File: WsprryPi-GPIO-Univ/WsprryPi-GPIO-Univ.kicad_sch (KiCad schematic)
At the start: 11 parts, among them J11 GPIO, J21 GPIO Select, J81 Conn_01x04, J82 Conn_01x04, J83 SMA_Adafruit_1865, SW11 Switch

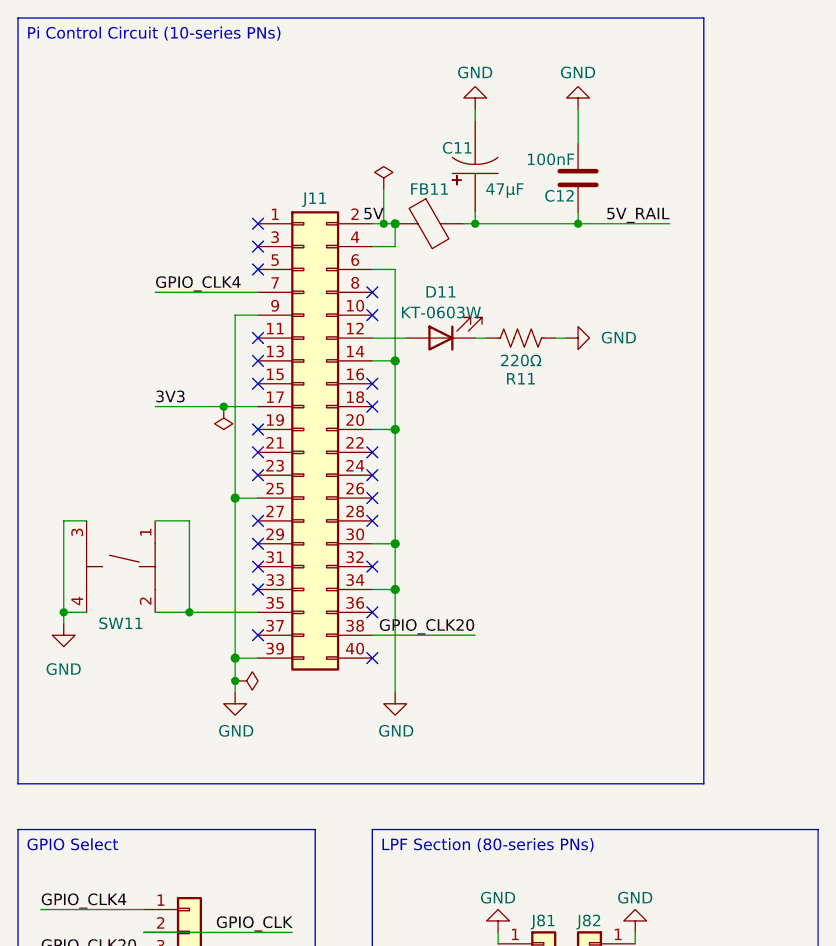
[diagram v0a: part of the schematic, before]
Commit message: Rename GPIO project and document amplifier requirements
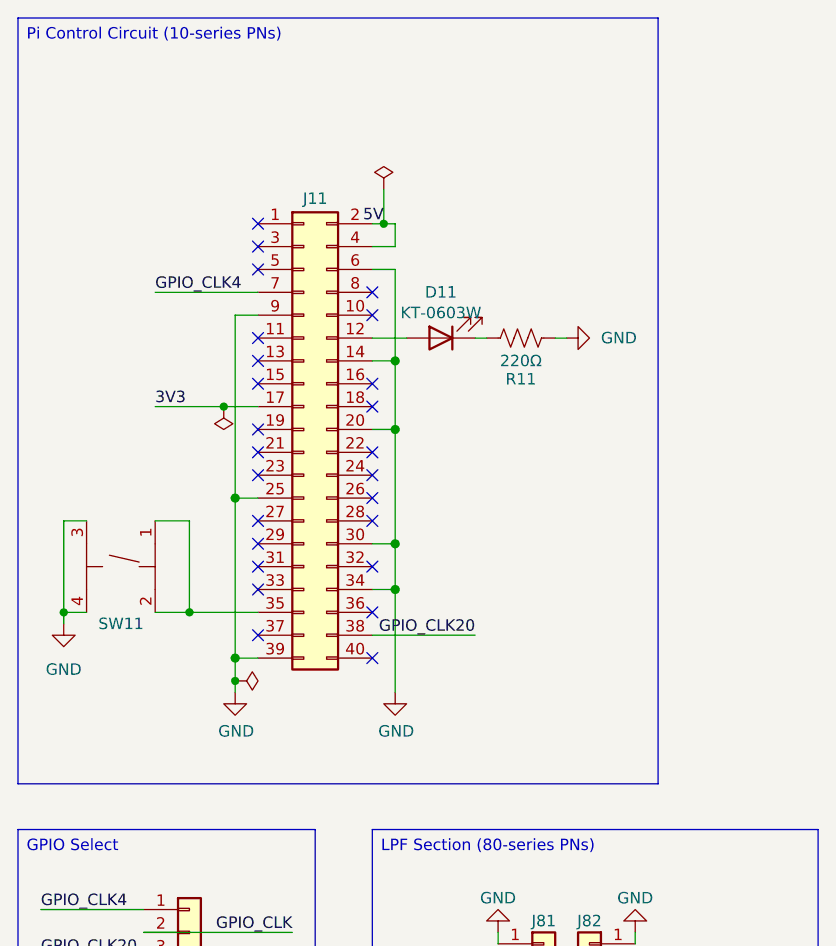
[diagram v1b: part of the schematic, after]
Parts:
- removed C11: 47µF, Wsprry Pi:CAP-SMD_BD6.3-L6.6-W6.6-FD, symbol Wsprry Pi:EEEFK1V470P
- removed C12: 100nF, Wsprry Pi:C_0603_1608Metric, symbol Wsprry Pi:C
- removed FB11: 600Ω@100MHz, Wsprry Pi:L_0603_1608Metric, symbol Wsprry Pi:FerriteBead

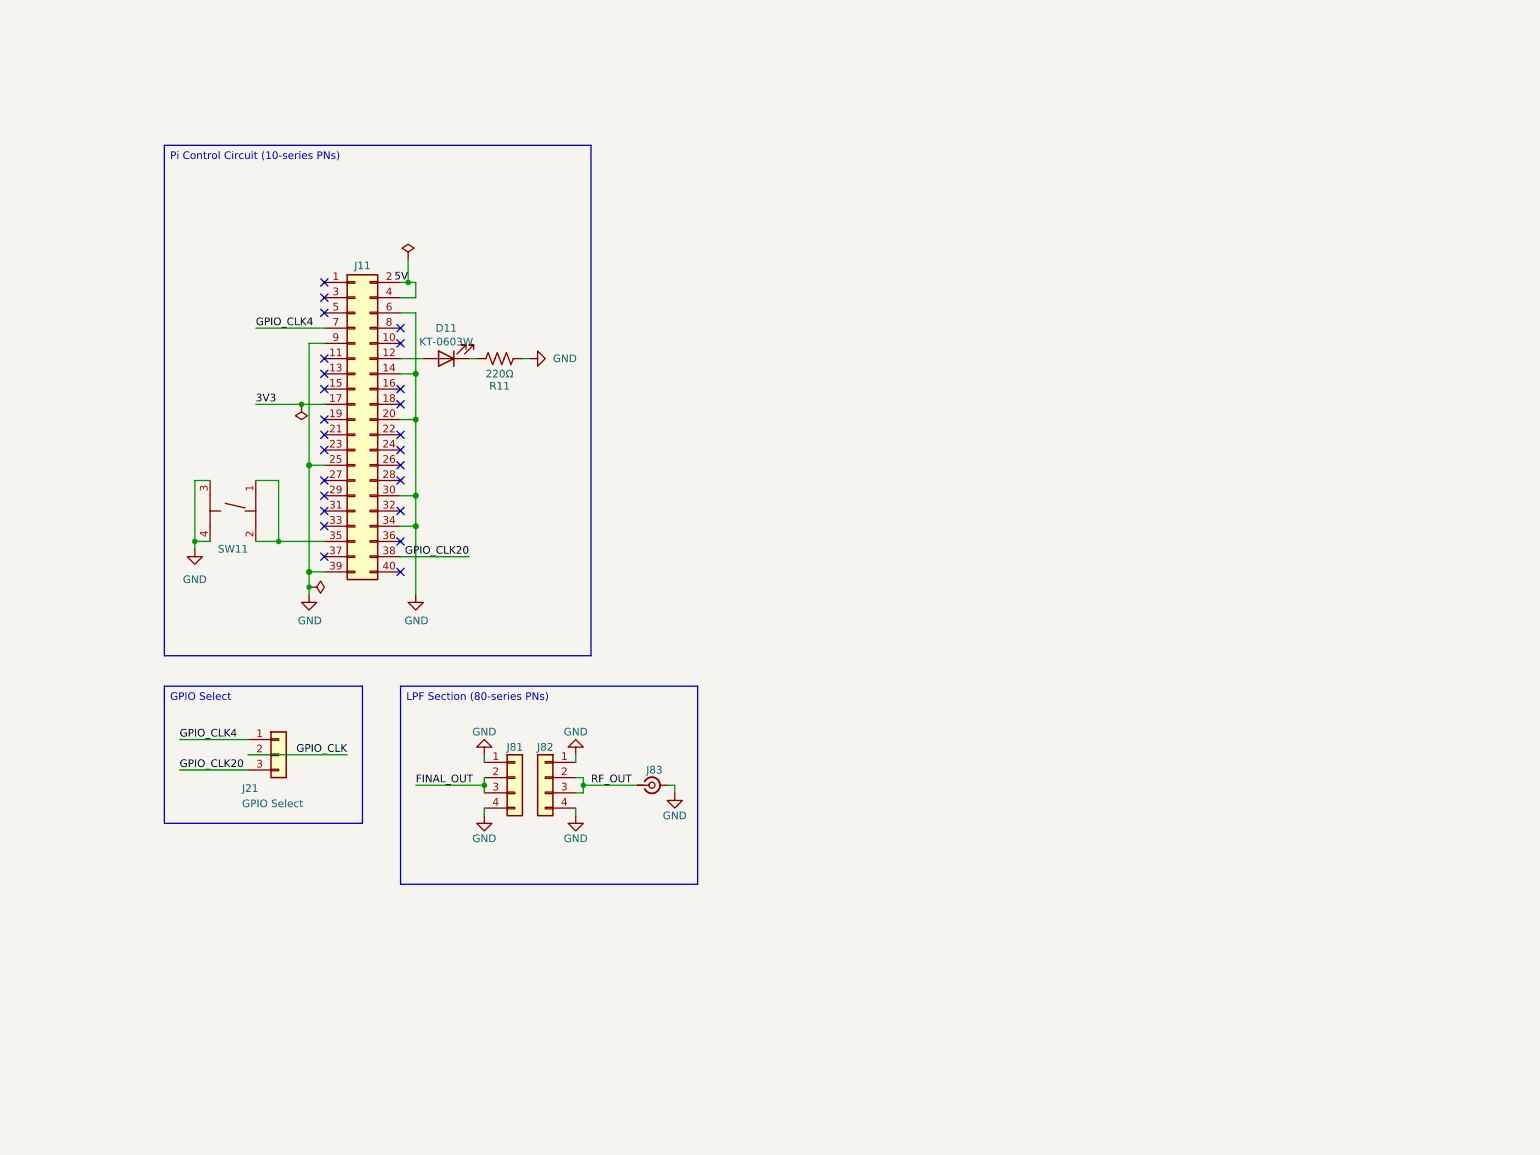
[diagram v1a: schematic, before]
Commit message: Add GPIO clock input buffer schematic
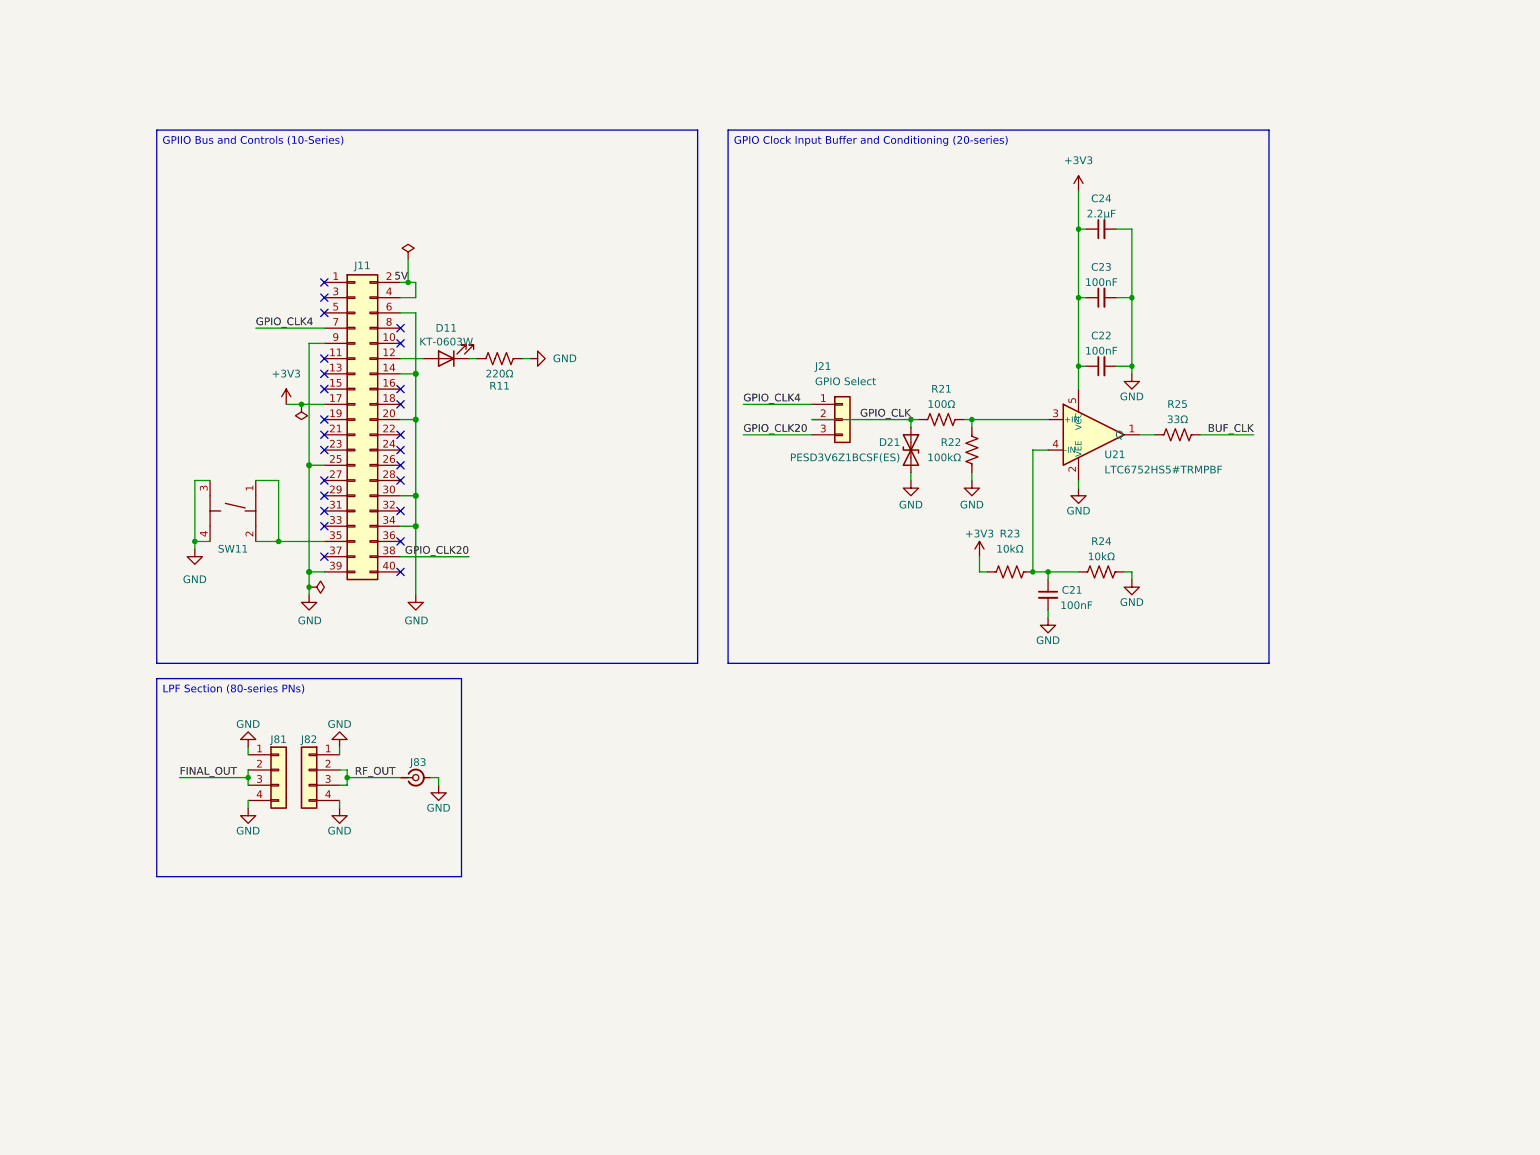
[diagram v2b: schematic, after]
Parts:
- added C21, C22, C23: 100nF, Capacitor_SMD:C_0402_1005Metric, symbol Device:C_Small
- added C24: 2.2µF, Capacitor_SMD:C_0603_1608Metric, symbol Device:C_Small
- added D21: PESD3V6Z1BCSF(ES), Wsprry Pi:DFN0603-2L_L0.62-W0.32-P0.40, symbol Wsprry Pi:PESD3V6Z1BCSF_ES
- added R21: 100Ω, Resistor_SMD:R_0603_1608Metric, symbol Wsprry Pi:R_US
- added R22: 100kΩ, Resistor_SMD:R_0603_1608Metric, symbol Wsprry Pi:R_US
- added R23, R24: 10kΩ, Resistor_SMD:R_0603_1608Metric, symbol Wsprry Pi:R_US
- added R25: 33Ω, Resistor_SMD:R_0603_1608Metric, symbol Wsprry Pi:R_US
- added U21: LTC6752HS5#TRMPBF, Wsprry Pi:TSOT-23-5, symbol Wsprry Pi:LTC6752HS5#TRMPBF
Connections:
- net GND: now also C21.2, C22.2, C23.2, C24.2, D21.2 (A2), R22.2, R24.2, U21.2 (VEE)
- net GPIO_CLK: now also D21.1 (A1), R21.1
- net 3V3 renamed +3V3
- net +3V3: now also C22.1, C23.1, C24.1, R23.1, U21.5 (VCC)
- new net: C21.1, R23.2, R24.1, U21.4 (-IN)
- new net: R25.1, U21.1 (Q)
- new net: R21.2, R22.1, U21.3 (+IN)
- new net BUF_CLK: R25.2
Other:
- moved on the sheet: J81, J82, J83

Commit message: Add GPIO broadband amplifier schematic blocks
Add the PA, bipolar supply, and protected Pi power-input circuitry, along with project-local symbols, footprints, and available STEP models. Localize all placed schematic symbols and assigned footprints.
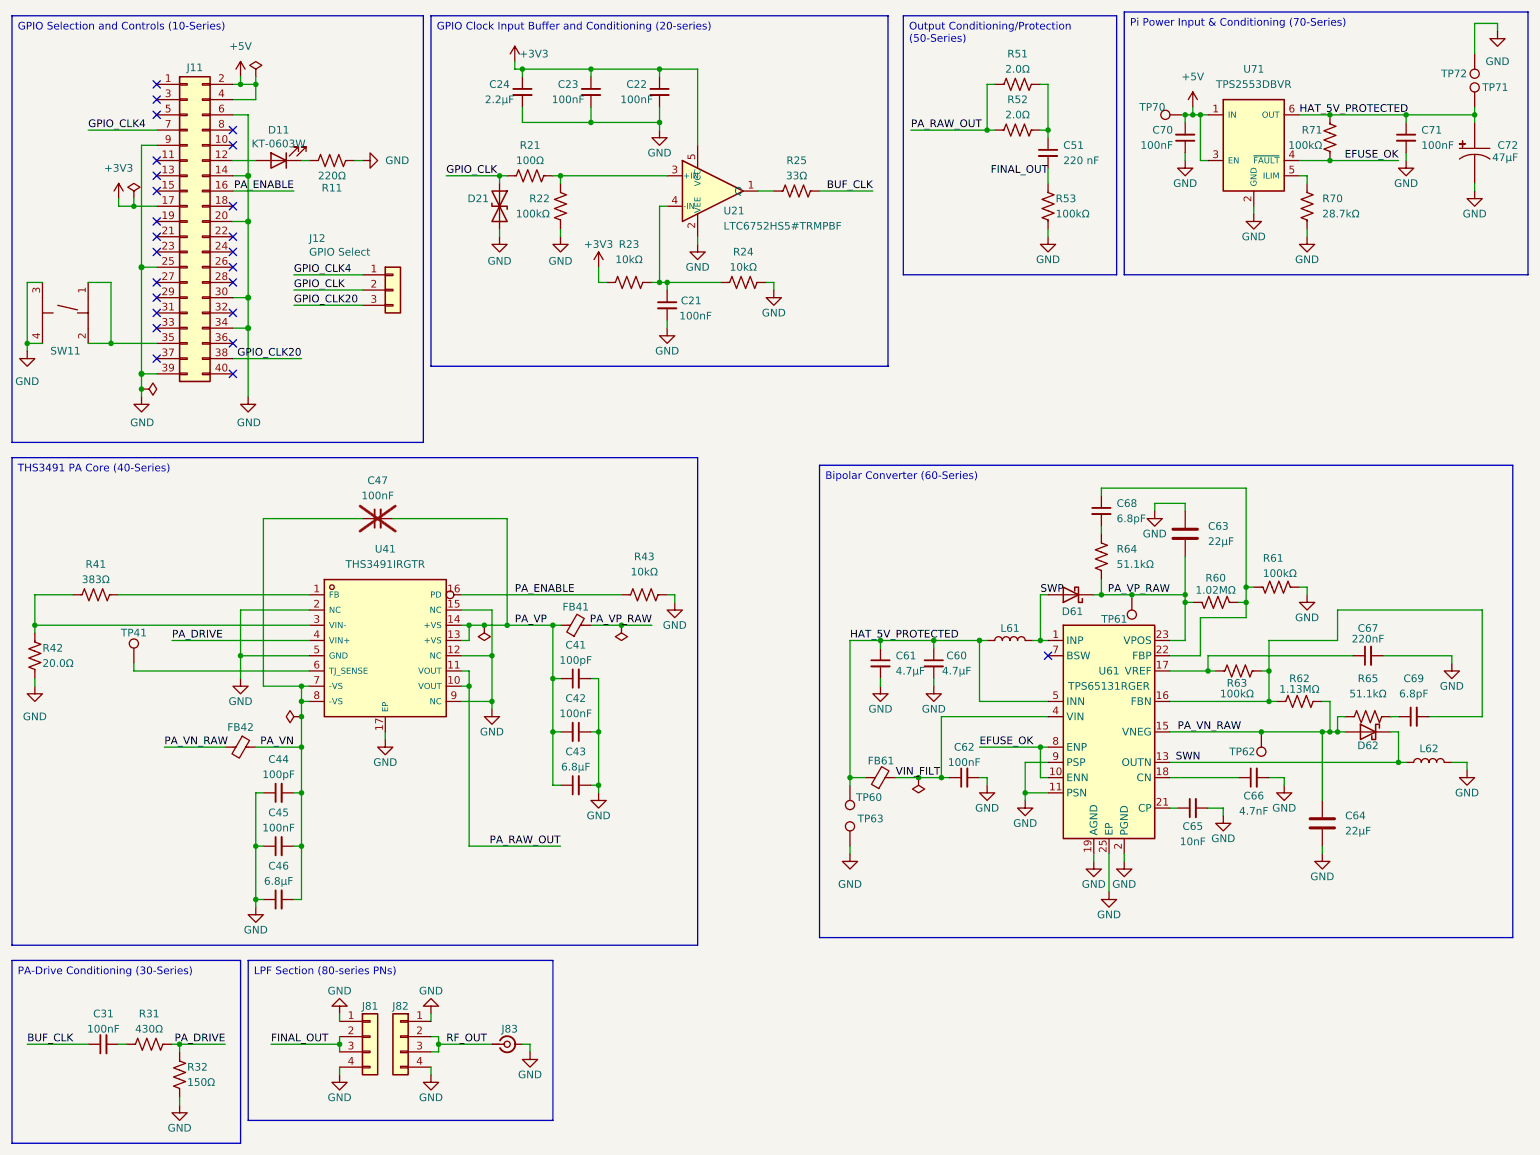
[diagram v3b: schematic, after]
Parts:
- removed J21: GPIO Select, Connector_PinHeader_1.00mm:PinHeader_1x03_P1.00mm_Vertical, symbol Connector_Generic:Conn_01x03
- added C31, C42, C45, C47, C62, C70, C71: 100nF, Wsprry Pi:C_0603_1608Metric, symbol Wsprry Pi:C_Small
- added C41, C44: 100pF, Wsprry Pi:C_0603_1608Metric, symbol Wsprry Pi:C_Small
- added C43, C46: 6.8µF, Wsprry Pi:C_1206_3216Metric, symbol Wsprry Pi:C_Small
- added C51: 220 nF, Wsprry Pi:C_1206_3216Metric, symbol Wsprry Pi:C_Small
- added C60, C61: 4.7µF, Wsprry Pi:C_1206_3216Metric, symbol Wsprry Pi:C_Small
- added C63, C64: 22µF, Wsprry Pi:C_1210_3225Metric, symbol Wsprry Pi:CL32B226KAJNNNE
- added C65: 10nF, Wsprry Pi:C_0603_1608Metric, symbol Wsprry Pi:C_Small
- added C66: 4.7nF, Wsprry Pi:C_0603_1608Metric, symbol Wsprry Pi:C_Small
- added C67: 220nF, Wsprry Pi:C_0603_1608Metric, symbol Wsprry Pi:C_Small
- added C68, C69: 6.8pF, Wsprry Pi:C_0603_1608Metric, symbol Wsprry Pi:C_Small
- added C72: 47µF, Wsprry Pi:CAP-SMD_BD6.3-L6.6-W6.6-FD, symbol Wsprry Pi:EEEFK1V470P
- added D61, D62: PMEG3020EP,115, Wsprry Pi:D_SOD-128, symbol Wsprry Pi:PMEG3020EP_115
- added FB41, FB42, FB61: BLM21PG221SN1D, Wsprry Pi:L_0805_2012Metric, symbol Wsprry Pi:BLM21PG221SN1D
- added J12: GPIO Select, Wsprry Pi:PinHeader_1x03_P1.00mm_Vertical, symbol Wsprry Pi:Conn_01x03
- added L61, L62: B82462G4472M000, Wsprry Pi:L_6.3x6.3_H3, symbol Wsprry Pi:B82462G4472M000
- added R31: 430Ω, Wsprry Pi:R_0603_1608Metric, symbol Wsprry Pi:R_US
- added R32: 150Ω, Wsprry Pi:R_0603_1608Metric, symbol Wsprry Pi:R_US
- added R41: 383Ω, Wsprry Pi:R_1206_3216Metric, symbol Wsprry Pi:R_US
- added R42: 20.0Ω, Wsprry Pi:R_0603_1608Metric, symbol Wsprry Pi:R_US
- added R43: 10kΩ, Wsprry Pi:R_0603_1608Metric, symbol Wsprry Pi:R_US
- added R51, R52: 2.0Ω, Wsprry Pi:R_1206_3216Metric, symbol Wsprry Pi:R_US
- added R53, R61, R63, R71: 100kΩ, Wsprry Pi:R_0603_1608Metric, symbol Wsprry Pi:R_US
- added R60: 1.02MΩ, Wsprry Pi:R_0603_1608Metric, symbol Wsprry Pi:R_US
- added R62: 1.13MΩ, Wsprry Pi:R_0603_1608Metric, symbol Wsprry Pi:R_US
- added R64, R65: 51.1kΩ, Wsprry Pi:R_0603_1608Metric, symbol Wsprry Pi:R_US
- added R70: 28.7kΩ, Wsprry Pi:R_0603_1608Metric, symbol Wsprry Pi:R_US
- added TP41, TP60, TP61, TP62, TP63, TP70, TP71, TP72: TestPoint, Wsprry Pi:TestPoint_Pad_D1.0mm, symbol Wsprry Pi:TestPoint
- added U41: THS3491IRGTR, Wsprry Pi:VQFN-16-1EP_3x3mm_P0.5mm_EP1.68x1.68mm_TI-RGT0016C_ThermalVias, symbol Wsprry Pi:THS3491IRGTR
- added U61: TPS65131RGER, Wsprry Pi:VQFN-24-1EP_4x4mm_P0.5mm_EP2.45x2.45mm_ThermalVias, symbol Wsprry Pi:TPS65131RGER
- added U71: TPS2553DBVR, Wsprry Pi:SOT-23-6_TI-DBV0006A, symbol Wsprry Pi:TPS2553DBVR
- C21, C22, C23: footprint Capacitor_SMD:C_0402_1005Metric -> Wsprry Pi:C_0402_1005Metric; symbol Device:C_Small -> Wsprry Pi:C_Small
- C24: footprint Capacitor_SMD:C_0603_1608Metric -> Wsprry Pi:C_0603_1608Metric; symbol Device:C_Small -> Wsprry Pi:C_Small
- R21, R22, R23, R24, R25: footprint Resistor_SMD:R_0603_1608Metric -> Wsprry Pi:R_0603_1608Metric
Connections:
- net BUF_CLK: now also C31.1
- net FINAL_OUT: now also C51.2, R53.1
- net GND: now also C41.2, C42.1, C43.2, C44.1, C45.1, C46.1, C60.2, C61.2, C62.2, C63.2, C64.2, C65.2, C66.2, C67.2, C70.1, C71.2, C72.2, L62.1, R32.2, R42.2, R43.2, R53.2, R61.1, R70.2, TP63.1, TP72.1, U41.12 (NC), U41.15 (NC), U41.17 (EP), U41.2 (NC), U41.5 (GND), U41.9 (NC), U61.11 (PSN), U61.19 (AGND), U61.2 (PGND), U61.25 (EP), U61.3 (PGND), U61.9 (PSP), U71.2 (GND)
- net GPIO_CLK: now also J12.2 (Pin_2)
- net GPIO_CLK20: now also J12.3 (Pin_3)
- net GPIO_CLK4: now also J12.1 (Pin_1)
- net PA_ENABLE: now reaches J11.16 (Pin_16)
- net PA_ENABLE: now also R43.1, U41.16 (PD)
- net 5V renamed +5V
- net +5V: now also C70.2, TP70.1, U71.1 (IN), U71.3 (EN)
- new net: C51.1, R51.2, R52.2
- new net: C67.1, R63.2, U61.17 (VREF)
- new net: R70.1, U71.5 (ILIM)
- new net: C69.2, R62.1, R63.1, U61.16 (FBN)
- new net: C66.1, U61.18 (CN)
- new net: C65.1, U61.21 (CP)
- new net: C68.1, R60.1, R61.2, U61.22 (FBP)
- new net: C69.1, R65.2
- new net: R41.2, U41.1 (FB)
- new net: R41.1, R42.1, U41.3 (VIN-)
- new net: TP41.1, U41.6 (TJ_SENSE)
- new net: C68.2, R64.1
- new net: C31.2, R31.1
- new net EFUSE_OK: R71.1, U61.10 (ENN), U61.8 (ENP), U71.4 (~{FAULT})
- new net HAT_5V_PROTECTED: C60.1, C61.1, C71.1, C72.1, FB61.1, L61.1, R71.2, TP60.1, TP71.1, U61.5 (INN), U61.6 (INN), U71.6 (OUT)
- new net PA_DRIVE: R31.2, R32.1, U41.4 (VIN+)
- new net PA_RAW_OUT: R51.1, R52.1, U41.10 (VOUT), U41.11 (VOUT)
- new net PA_VN: C44.2, C45.2, C46.2, C47.1, FB42.1, U41.7 (-VS), U41.8 (-VS)
- new net PA_VN_RAW: C64.1, D62.2 (A), FB42.2, R62.2, R65.1, TP62.1, U61.15 (VNEG)
- new net PA_VP: C41.1, C42.2, C43.1, C47.2, FB41.1, U41.13 (+VS), U41.14 (+VS)
- new net PA_VP_RAW: C63.1, D61.1 (K), FB41.2, R60.2, R64.2, TP61.1, U61.23 (VPOS)
- new net SWN: D62.1 (K), L62.2, U61.13 (OUTN), U61.14 (OUTN)
- new net SWP: D61.2 (A), L61.2, U61.1 (INP), U61.24 (INP)
- new net VIN_FILT: C62.1, FB61.2, U61.4 (VIN)
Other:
- moved on the sheet: C21, C22, C23, C24, D11, D21, J11, J81, J82, J83, R11, R21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
